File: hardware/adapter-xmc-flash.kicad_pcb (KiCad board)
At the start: 2 copper layers, 95 x 50 mm, 26 parts, among them J1 USB-MINI-B-SMD, P1 CON-SENSOR, P2 CON-SENSOR2, P3 CONN_01X07, P4 CON-SENSOR, P5 CON-SENSOR, U1 CP2104, U2 M24C64, U3 CPC1020N, U4 CPC1020N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

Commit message: PCB optimizations
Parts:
- added G***: Logo_31x31, kicad-libraries:Logo_31x31, F.Cu at (187.8, 98.5)
- added G***: LOGO, kicad-libraries:Logo_CoMCU, F.Cu at (189.3, 94.3)
- moved P3 38.3 mm to (151.3, 113.6)
- moved R4 38.3 mm to (131.1, 114.1)
- moved R5 38.3 mm to (131.1, 119.1)
- moved U3 38.3 mm to (137.3, 118.3)
- moved U4 38.3 mm to (137.3, 113.3)
- moved C1 38.3 mm to (172.6, 90.6)
- moved C2 38.3 mm to (172.6, 92.1)
- moved C3 38.3 mm to (177.1, 97.1)
- moved C4 38.3 mm to (177.8, 88.6)
- moved C5 38.3 mm to (178.6, 87.1)
- moved C6 38.3 mm to (120.8, 110.1)
- moved D1 38.3 mm to (182.8, 85.1)
- moved J1 38.3 mm to (182.6, 74.1)
- moved P1 38.3 mm to (162.8, 123.6)
- moved P2 38.3 mm to (177.1, 123.8)
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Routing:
- net TX_RIN: track 70.7 -> 52.5 mm
- net GND: track 42.9 -> 37.0 mm
- net Net-(P1-Pad10): track 98.1 -> 95.3 mm, vias 3 -> 4
- net RXD: track 118.6 -> 116.0 mm, vias 5 -> 6
- net Net-(C4-Pad1): track 22.1 -> 19.7 mm
- net TX_ROUT: track 102.0 -> 100.2 mm
- net POWER_ROUT: track 44.9 -> 43.3 mm
- net Net-(J1-Pad3): track 13.6 -> 12.1 mm
- net Net-(P1-Pad7): track 92.8 -> 91.3 mm, vias 3 -> 5
- net 3V3: track 98.8 -> 97.5 mm
- net Net-(P1-Pad1): track 96.2 -> 96.0 mm, vias 1 -> 3
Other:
- board text added: "1.0"
- board text added: "Flash Adapter XMC"
- board text removed: "XMC1400 Breakout"

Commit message: Add socket markings
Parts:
- moved R3 2.50 mm to (114.5, 104.1)
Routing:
- net Net-(P5-Pad3): track 4.73 -> 7.23 mm
- net 3V3: track 97.5 -> 95.0 mm
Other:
- board text added: "3,3V"
- board text added: "5V"
- board text added: "Bricklet"
- board text added: "CLK/TX"
- board text added: "CS"
- board text added: "GND"
- board text added: "MISO"
- board text added: "MOSI/RX"
- board text added: "control"
- board text added: "program"
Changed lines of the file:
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@@
     (links 74)
     (no_connects 0)
-    (area 66.609499 89.909499 161.990501 140.290501)
+    (area 101.359499 73.909499 196.740501 124.290501)
     (thickness 1.6002)
-    (drawings 116)
+    (drawings 126)
     (tracks 321)
     (zones 0)
@@
   (title_block
     (title "Flash Adapter XMC")
-    (date 2017-02-08)
+    (date 2017-02-09)
     (rev 1.0)
     (company "Tinkerforge GmbH")
@@
   )
   (setup
-    (last_trace_width 0.25)
+    (last_trace_width 0.2)
     (user_trace_width 0.25)
     (user_trace_width 0.29972)
@@
     (descr "Connecteur 7 pins")
     (tags "CONN DEV")
-    (fp_text reference P3 (at 1.27 -2.159 90) (layer F.SilkS)
+    (fp_text reference P3 (at -3.75 0 180) (layer F.SilkS)
       (effects (font (size 1.016 1.016) (thickness 0.2032)))
     )
@@
   )
   (module 0603F (layer Vorderseite)
-    (at 112.05 104.1 180)
+    (at 114.55 104.1 180)
     (attr smd)
     (fp_text reference R3 (at 0.05 0.225 180) (layer F.SilkS)
@@
       (xy 1.301301 -2.715081) (xy 1.302426 -2.714986)) (layer F.SilkS) (width 0.01))
   )
+  (gr_text MISO (at 155.8 105.85) (layer F.SilkS)
+    (effects (font (size 1 1) (thickness 0.15)))
+  )
+  (gr_text MOSI/RX (at 157.3 108.6) (layer F.SilkS)
+    (effects (font (size 1 1) (thickness 0.15)))
+  )
+  (gr_text CLK/TX (at 156.8 111.1) (layer F.SilkS)
+    (effects (font (size 1 1) (thickness 0.15)))
+  )
+  (gr_text CS (at 155.05 113.6) (layer F.SilkS)
+    (effects (font (size 1 1) (thickness 0.15)))
+  )
+  (gr_text 3,3V (at 155.55 116.1) (layer F.SilkS)
+    (effects (font (size 1 1) (thickness 0.15)))
+  )
+  (gr_text GND (at 155.3 118.6) (layer F.SilkS)
+    (effects (font (size 1 1) (thickness 0.15)))
+  )
+  (gr_text 5V (at 154.8 121.1) (layer F.SilkS)
+    (effects (font (size 1 1) (thickness 0.15)))
+  )
+  (gr_text control (at 110.3 106.6 270) (layer F.SilkS)
+    (effects (font (size 2 2) (thickness 0.3048)))
+  )
+  (gr_text program (at 110.3 88.1 270) (layer F.SilkS)
+    (effects (font (size 2 2) (thickness 0.3048)))
+  )
+  (gr_text Bricklet (at 169.8 115.1) (layer F.SilkS)
+    (effects (font (size 2 2) (thickness 0.3048)))
+  )
   (gr_text 1.0 (at 194.15 116.5) (layer F.SilkS)
     (effects (font (size 0.8 0.8) (thickness 0.15)))
@@
   (segment (start 131.05 113.1) (end 128.05 110.1) (width 0.25) (layer Vorderseite) (net 5))
   (segment (start 128.05 110.1) (end 121.55 110.1) (width 0.25) (layer Vorderseite) (net 5))
-  (segment (start 112.8 104.1) (end 119.05 104.1) (width 0.25) (layer Vorderseite) (net 5))
+  (segment (start 115.3 104.1) (end 119.05 104.1) (width 0.25) (layer Vorderseite) (net 5) (status 400000))
   (segment (start 119.05 104.1) (end 119.05 104.1) (width 0.25) (layer Vorderseite) (net 5))
   (segment (start 119.05 104.1) (end 121.55 106.6) (width 0.25) (layer Vorderseite) (net 5))
@@
   (segment (start 136.3 117.1) (end 136.3 111.35) (width 0.25) (layer Vorderseite) (net 19))
   (segment (start 138.185 118.985) (end 136.3 117.1) (width 0.25) (layer Vorderseite) (net 19))
-  (segment (start 106.5752 104.10064) (end 111.29936 104.10064) (width 0.25) (layer Vorderseite) (net 24))
-  (segment (start 111.29936 104.10064) (end 111.3 104.1) (width 0.25) (layer Vorderseite) (net 24))
+  (segment (start 106.5752 104.10064) (end 113.8 104.1) (width 0.25) (layer Vorderseite) (net 24) (status C00000))
+  (segment (start 113.8 104.1) (end 113.80064 104.09936) (width 0.25) (layer Vorderseite) (net 24) (status 400000))
   (segment (start 106.5752 105.09886) (end 109.04886 105.09886) (width 0.2) (layer Vorderseite) (net 25))
   (segment (start 118.93246 114.23246) (end 121.49748 114.23246) (width 0.2) (layer Vorderseite) (net 25))

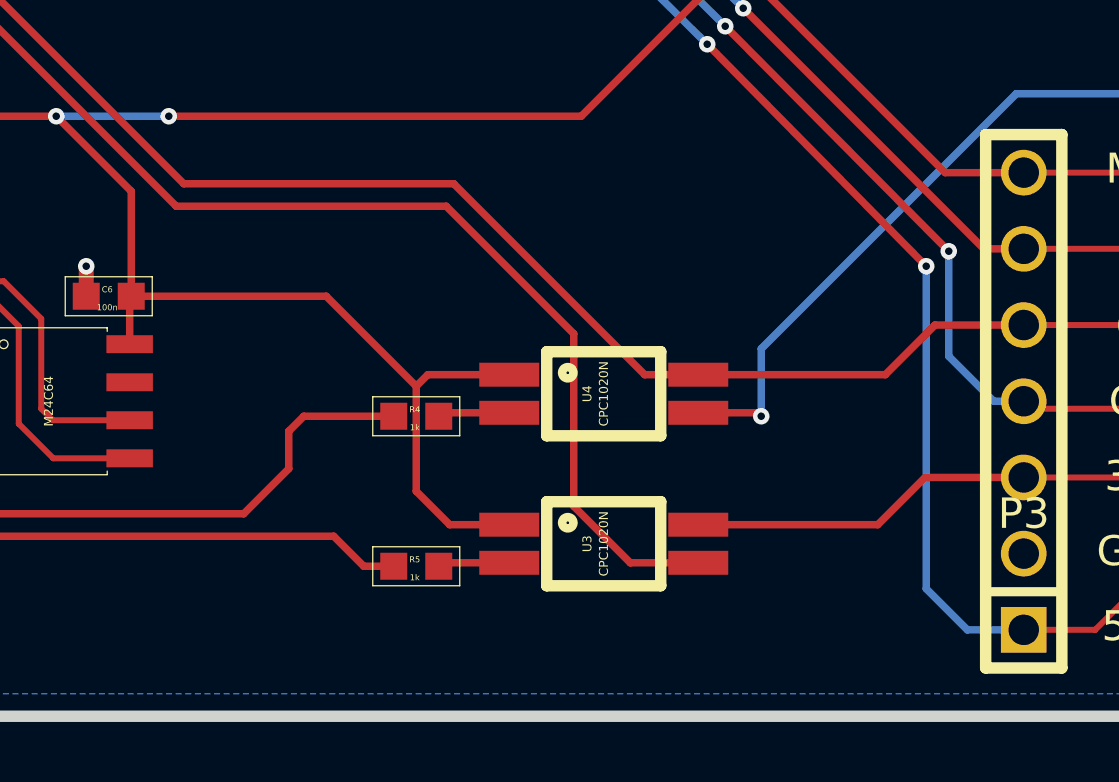
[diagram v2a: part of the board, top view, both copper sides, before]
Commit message: fix solid state footprints
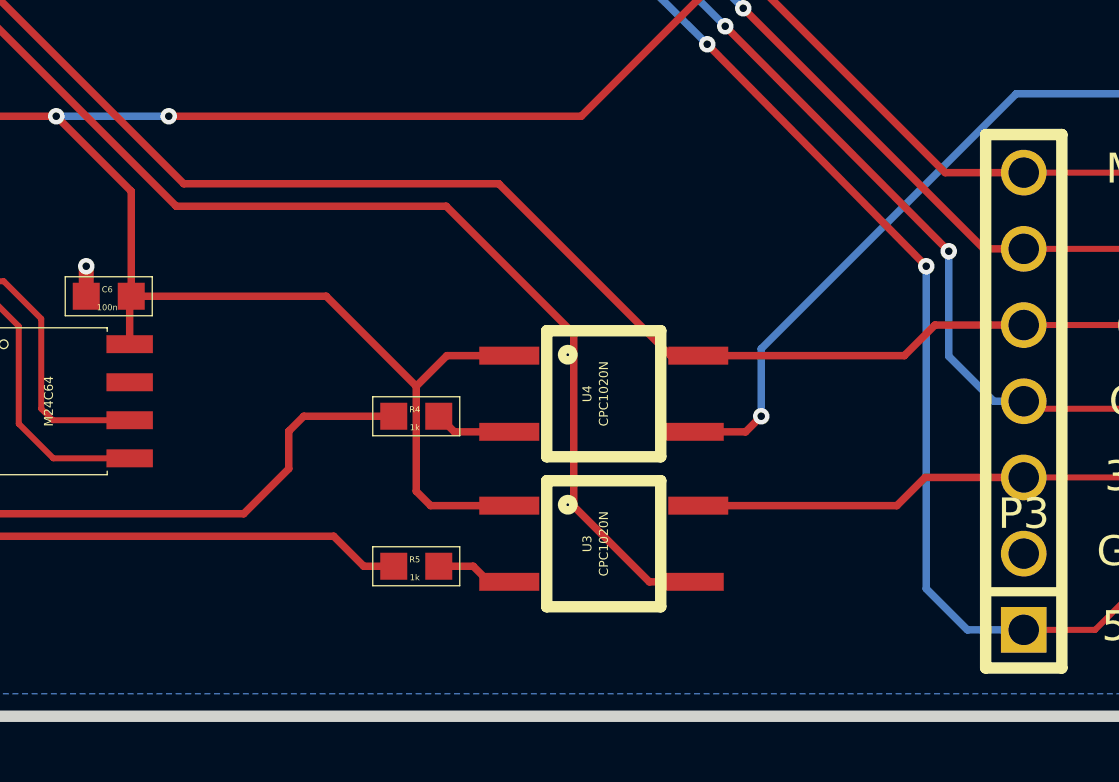
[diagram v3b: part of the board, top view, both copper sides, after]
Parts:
- U3, U4: footprint SOP4 -> SOP4-WIDE
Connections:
- J1 pad 4: Net-(J1-Pad4) -> (no net)
- P1 pad 4: Net-(P1-Pad4) -> (no net)
- P1 pad 5: Net-(P1-Pad5) -> (no net)
- P1 pad 6: Net-(P1-Pad6) -> (no net)
- P4 pad 4: Net-(P4-Pad4) -> (no net)
- P4 pad 5: Net-(P4-Pad5) -> (no net)
- P4 pad 6: Net-(P4-Pad6) -> (no net)
- P5 pad 1: Net-(P5-Pad1) -> (no net)
- P5 pad 10: Net-(P5-Pad10) -> (no net)
- P5 pad 9: Net-(P5-Pad9) -> (no net)
- U1 pad 1: Net-(U1-Pad1) -> (no net)
- U1 pad 10: Net-(U1-Pad10) -> (no net)
- U1 pad 11: Net-(U1-Pad11) -> (no net)
- U1 pad 12: Net-(U1-Pad12) -> (no net)
- U1 pad 13: Net-(U1-Pad13) -> (no net)
- U1 pad 14: Net-(U1-Pad14) -> (no net)
- U1 pad 15: Net-(U1-Pad15) -> (no net)
- U1 pad 17: Net-(U1-Pad17) -> (no net)
- U1 pad 18: Net-(U1-Pad18) -> (no net)
- U1 pad 19: Net-(U1-Pad19) -> (no net)
- U1 pad 22: Net-(U1-Pad22) -> (no net)
- U1 pad 23: Net-(U1-Pad23) -> (no net)
- U1 pad 24: Net-(U1-Pad24) -> (no net)
- U2 pad 7: Net-(U2-Pad7) -> (no net)
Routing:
- net TX_ROUT: track 100.2 -> 99.7 mm

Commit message: delete bottom silkscreen stuff
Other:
- board text removed: "1"
- board text removed: "2"
- board text removed: "3"
- board text removed: "4"
- board text removed: "Full-Duplex Non-Terminated"
- board text removed: "Full-Duplex Terminated"
- board text removed: "Half-Duplex Non-Terminated"
- board text removed: "Half-Duplex Terminated"
- board text removed: "ON"

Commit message: Minor adjustments
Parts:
- C1, C2, C5, C6: footprint 0603F -> kicad-libraries:C0603F
- C3, C4: footprint 0805 -> kicad-libraries:C0805
- D1: footprint SOD-123 -> kicad-libraries:SOD-123
- J1: footprint USB-MINI-B-SMD -> kicad-libraries:USB-MINI-B-SMD
- P1, P4, P5: footprint CON-SENSOR -> kicad-libraries:CON-SENSOR
- P2: footprint CON-SENSOR2 -> kicad-libraries:CON-SENSOR2
- P3: footprint PIN_ARRAY-7X1 -> kicad-libraries:PIN_ARRAY-7X1
- R1, R2, R3, R4, R5: footprint 0603F -> kicad-libraries:R0603F
- U1: footprint QFN-24-4x4-EP -> kicad-libraries:QFN-24-4x4-EP
- U2: footprint SOIC8 -> kicad-libraries:SOIC8
- U3, U4: footprint SOP4-WIDE -> kicad-libraries:SOP4-WIDE
- U5, U6, U7, U8: footprint DRILL_NP -> kicad-libraries:DRILL_NP
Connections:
- J1 pad 4: (no net) -> Net-(J1-Pad4)
- P1 pad 4: (no net) -> Net-(P1-Pad4)
- P1 pad 5: (no net) -> Net-(P1-Pad5)
- P1 pad 6: (no net) -> Net-(P1-Pad6)
- P4 pad 4: (no net) -> Net-(P4-Pad4)
- P4 pad 5: (no net) -> Net-(P4-Pad5)
- P4 pad 6: (no net) -> Net-(P4-Pad6)
- P5 pad 1: (no net) -> Net-(P5-Pad1)
- P5 pad 10: (no net) -> Net-(P5-Pad10)
- P5 pad 9: (no net) -> Net-(P5-Pad9)
- U1 pad 1: (no net) -> Net-(U1-Pad1)
- U1 pad 10: (no net) -> Net-(U1-Pad10)
- U1 pad 11: (no net) -> Net-(U1-Pad11)
- U1 pad 12: (no net) -> Net-(U1-Pad12)
- U1 pad 13: (no net) -> Net-(U1-Pad13)
- U1 pad 14: (no net) -> Net-(U1-Pad14)
- U1 pad 15: (no net) -> Net-(U1-Pad15)
- U1 pad 17: (no net) -> Net-(U1-Pad17)
- U1 pad 18: (no net) -> Net-(U1-Pad18)
- U1 pad 19: (no net) -> Net-(U1-Pad19)
- U1 pad 22: (no net) -> Net-(U1-Pad22)
- U1 pad 23: (no net) -> Net-(U1-Pad23)
- U1 pad 24: (no net) -> Net-(U1-Pad24)
- U2 pad 7: (no net) -> Net-(U2-Pad7)
